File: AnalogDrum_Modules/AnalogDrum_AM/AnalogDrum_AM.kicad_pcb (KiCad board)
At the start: 2 copper layers, 100.3 x 160 mm, 143 parts, among them J101 Conn_01x05_Male, Q301 2N3904, Q302 2N3904, Q303 2N3904, Q501 2N3904, Q502 2N3904, Q503 2N3904, SW101 SW_SPDT, SW401 SW_DPDT_x2, SW402 SW_DPDT_x2, U201 NE5532, U202 LM13700, U203 NE5532, U301 TL074, U302 LM358, U401 TL074, U501 TL074, U502 LM358

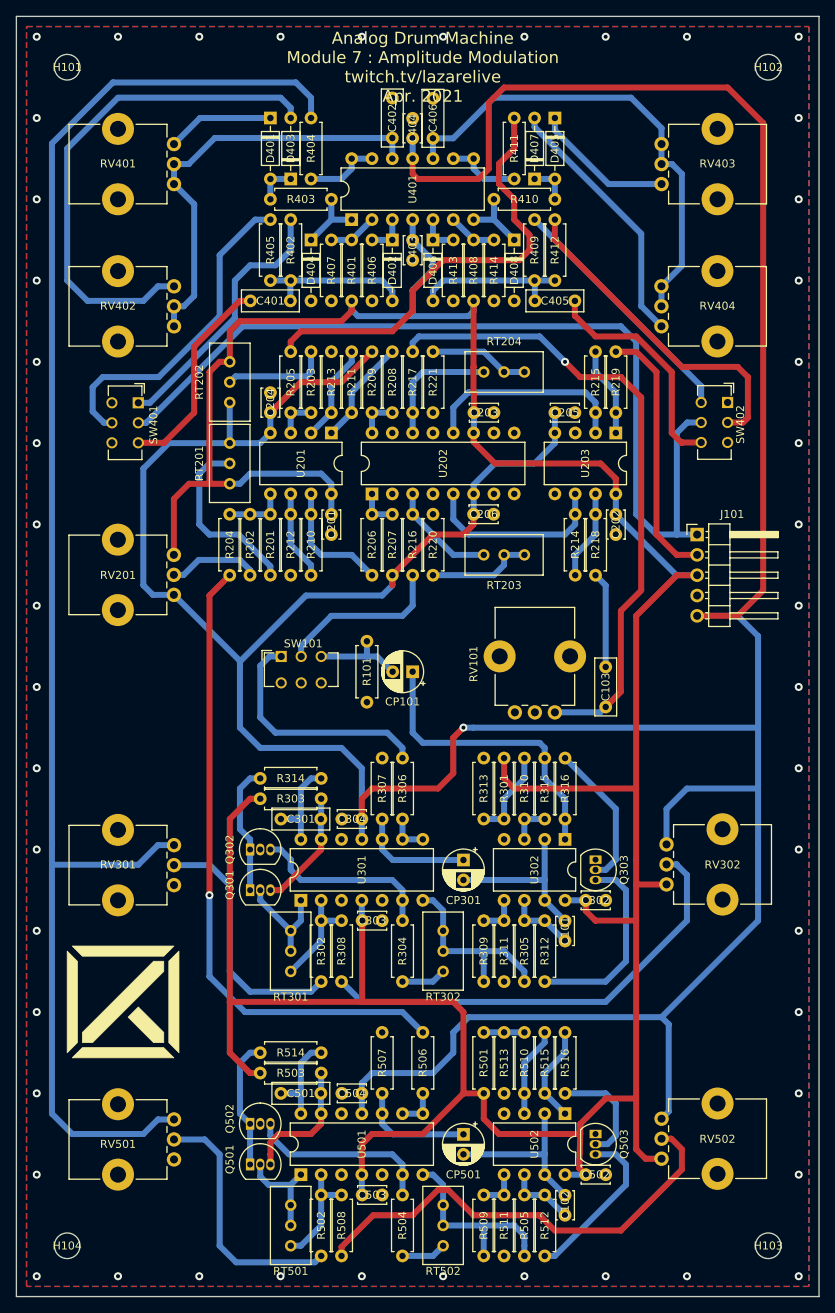
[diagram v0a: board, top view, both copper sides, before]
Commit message: Version 0.1.1
Corrections mineures :
- Vérification des potentiomètres
- Passage des connecteurs de carte e n JST
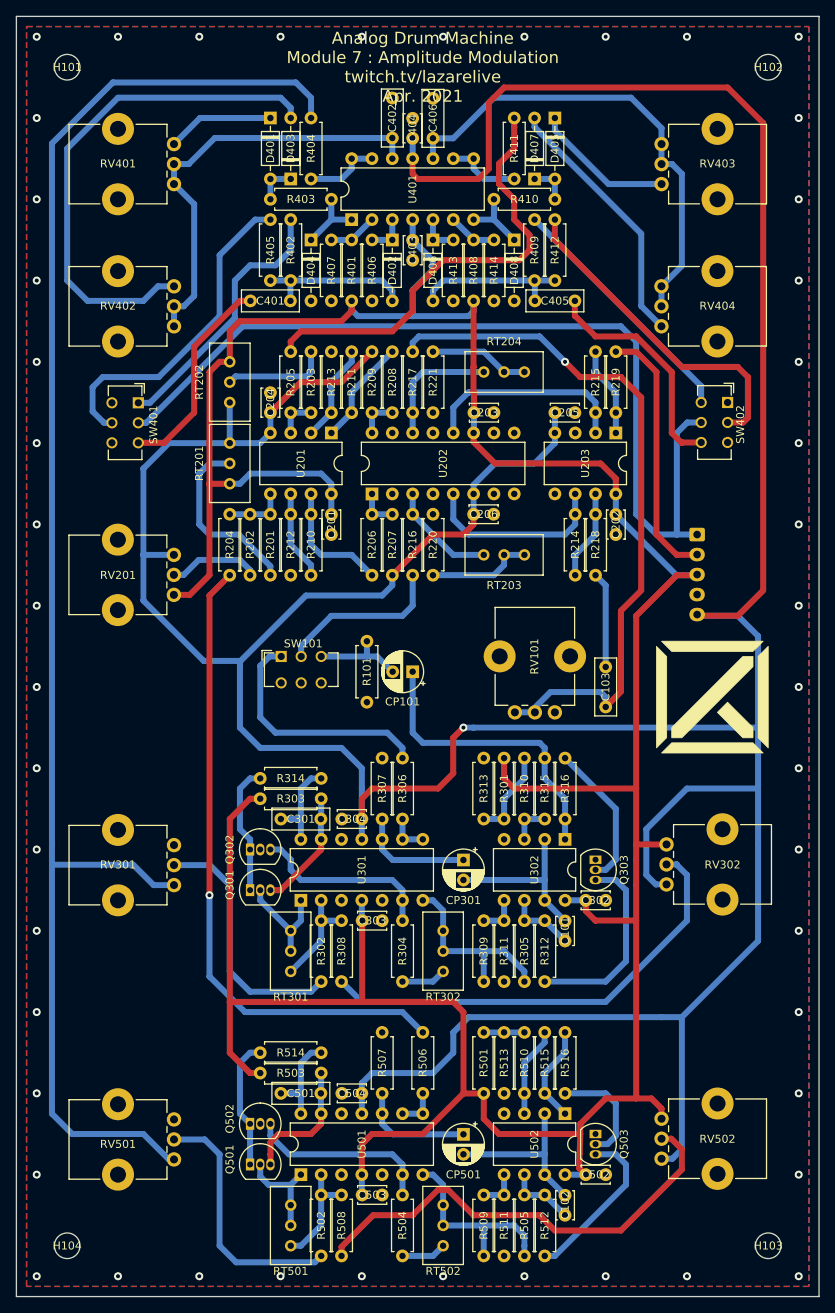
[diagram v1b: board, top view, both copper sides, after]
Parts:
- J101: footprint Connector_PinHeader_2.54mm:PinHeader_1x05_P2.54mm_Horizontal -> Connector_JST:JST_EH_B5B-EH-A_1x05_P2.50mm_Vertical; moved to B.Cu
- moved REF** 82.9 mm to (155.6, 102.9)
- turned J101 to 270 degrees
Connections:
- RV101 pad 1: /VCA/SIGB_IN -> GNDA
- RV101 pad 2: GNDA -> /VCA/SIGB_IN
- RV101 pad 3: GNDA -> /VCA/SIGB_IN
- RV201 pad 1: +12V -> -12V
- RV201 pad 3: -12V -> +12V
- RV301 pad 1: /EG/EGA_OUT -> GNDA
- RV301 pad 3: GNDA -> /EG/EGA_OUT
- RV302 pad 1: +12V -> -12V
- RV302 pad 3: -12V -> +12V
- RV501 pad 1: /EG/EGA_OUT -> GNDA
- RV501 pad 3: GNDA -> /EG/EGA_OUT
- RV502 pad 1: +12V -> -12V
- RV502 pad 3: -12V -> +12V
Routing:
- net -12V: track 489.8 -> 509.0 mm
- net /VCA/SIGB_IN: track 80.3 -> 88.0 mm
- net /EG/EGA_OUT: track 193.5 -> 194.1 mm
